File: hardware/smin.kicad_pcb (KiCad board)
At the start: 2 copper layers, 36 parts, among them P1 ISP, P2 CONN_1, Q1 BSS84, SW1 SW_DIP_8, SW2 SW_PUSH, U1 MINIMUS, U2 MINIMUS, U3 CD4050, U4 74HC243, U5 ZIF, U6 NCP1117, U7 AT45DB, X1 PIEZO

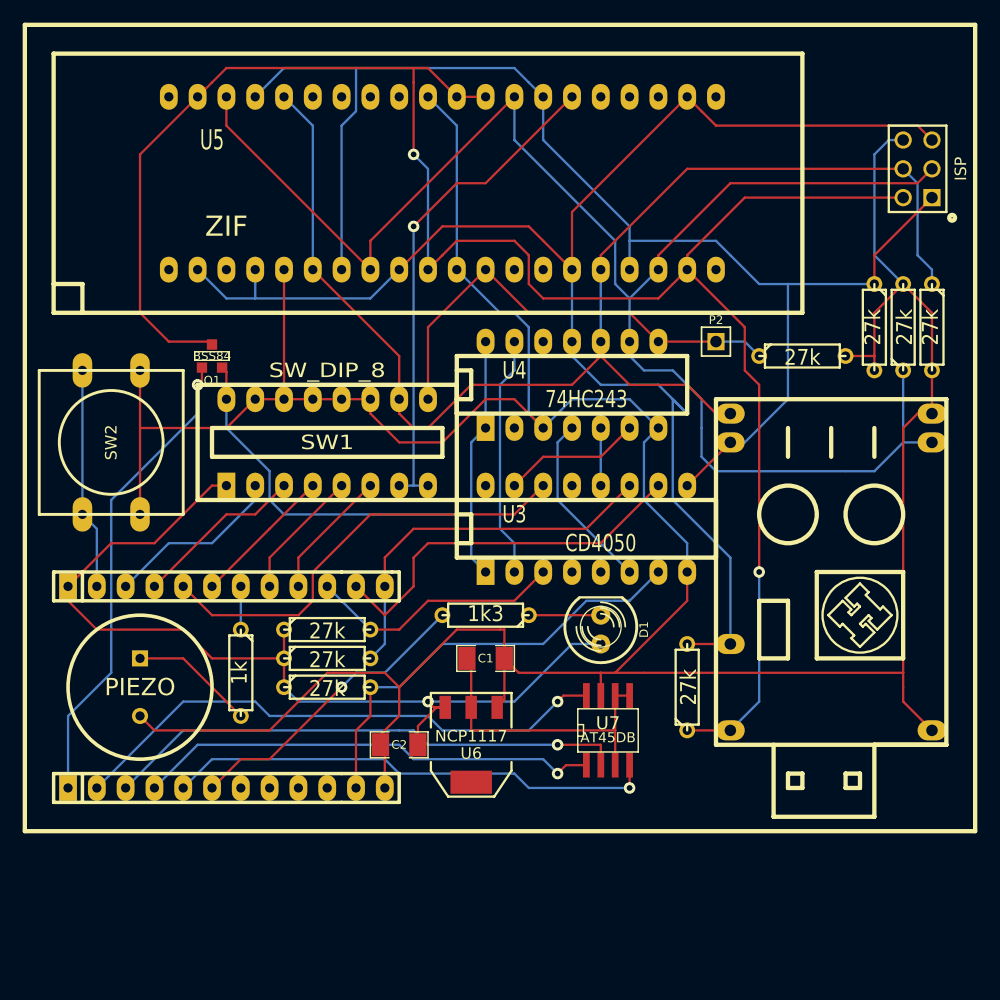
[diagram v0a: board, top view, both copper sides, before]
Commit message: PCB fixes
Signed-off-by: Paul Brook <paul@nowt.org>
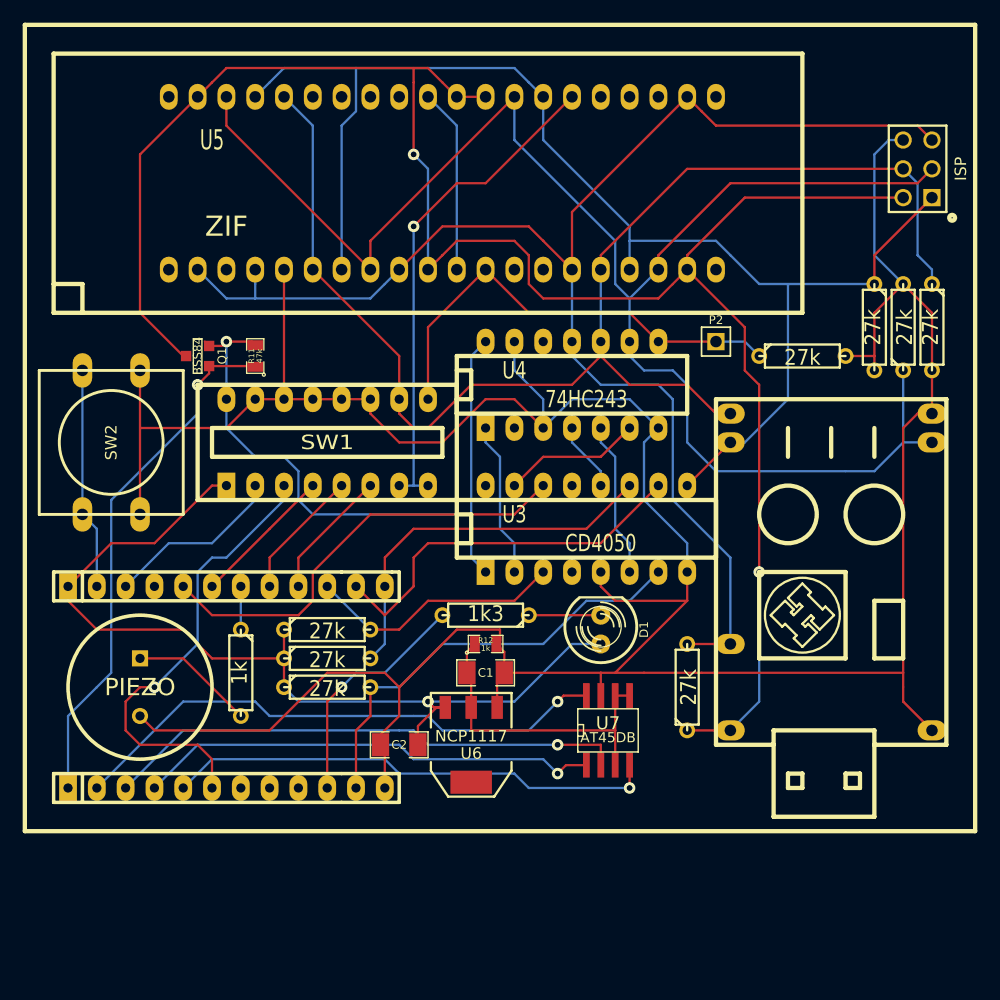
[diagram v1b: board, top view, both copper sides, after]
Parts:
- added R11: 47k, SM0805, F.Cu at (45.7, 54.6)
- added R12: 1k, SM0805, F.Cu at (66.0, 80.0)
- SW2: footprint SW_PUSH-12mm -> SW_PUSH-12
- moved LOGO_SMALL 5.08 mm to (94.0, 77.5)
- moved C1 1.27 mm to (66.0, 82.5)
- moved Q1 1.27 mm to (40.6, 54.6), turned to 270 degrees
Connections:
- R10 pad 2: N-0000026 (its old number) -> N-0000014
- U1 pad 10: (no net) -> N-0000014
- U1 pad 6: N-0000026 (its old number) -> /CFG3
- U2 pad 4: /CFG3 -> (no net)
- U3 pad 12: N-0000028 (its old number) -> N-000009
- U3 pad 5: (no net) -> GND
- U3 pad 6: N-0000013 (its old number) -> N-0000022
- U4 pad 1: /VCC -> N-0000053
- U4 pad 13: N-0000053 -> GND
- U4 pad 4: N-0000013 (its old number) -> N-000009
- U4 pad 5: N-0000028 (its old number) -> N-0000022
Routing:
- net N-0000026 (its old number): track 26.6 -> 0.00 mm, vias 1 -> 0
- net /CFG3: track 15.1 -> 40.1 mm, vias 0 -> 1
- net N-0000014: track 0.00 -> 20.9 mm, vias 0 -> 1
- net N-0000013 (its old number): track 15.9 -> 0.00 mm
- net N-0000022: track 0.00 -> 13.8 mm
- net N-0000053: track 21.4 -> 13.8 mm
- net /VCC: track 53.1 -> 60.1 mm, vias 0 -> 1
- net N-000009: track 0.00 -> 6.13 mm
- net N-0000028 (its old number): track 5.08 -> 0.00 mm
- net N-0000031: track 42.0 -> 46.5 mm
- net RST: track 132.6 -> 129.0 mm
- net +3.3V: track 26.1 -> 28.2 mm
- net Vt: track 173.6 -> 171.7 mm

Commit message: First pass at rev2 hardware
Signed-off-by: Paul Brook <paul@nowt.org>
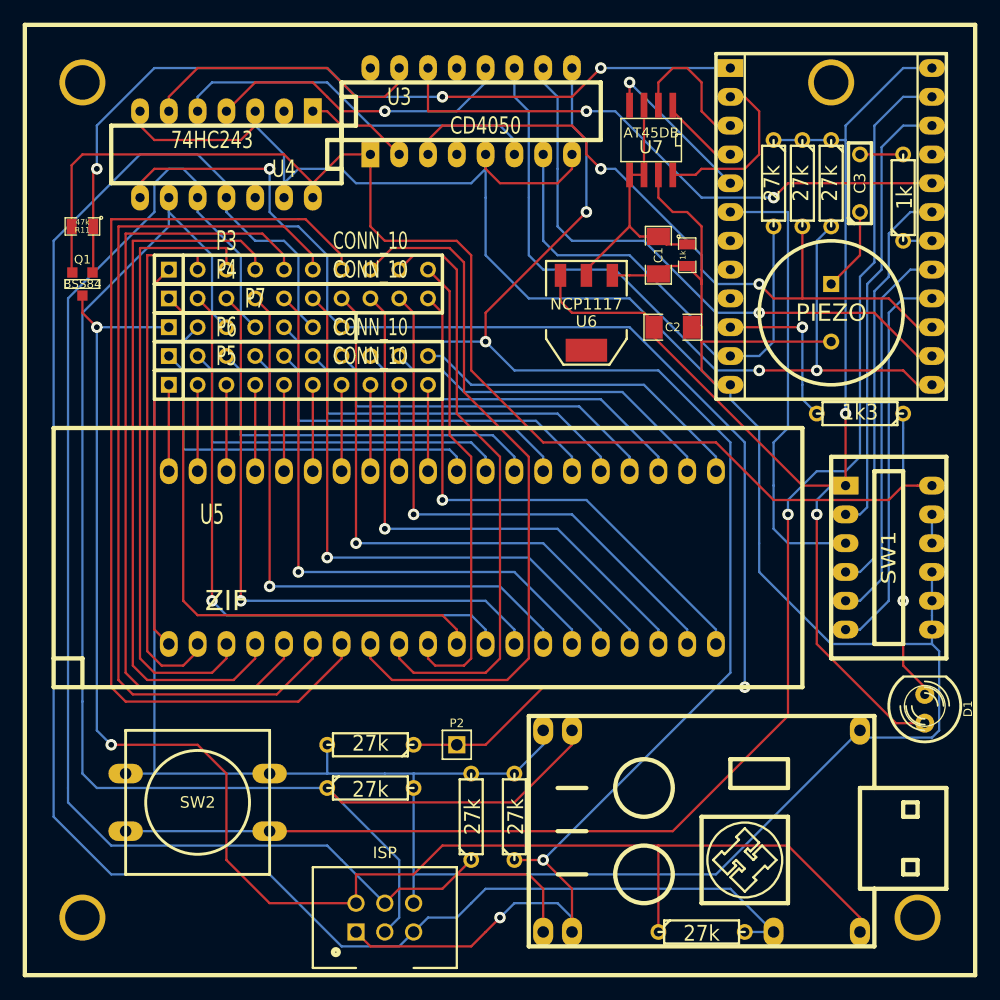
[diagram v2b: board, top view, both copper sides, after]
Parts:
- removed U2: MINIMUS, SIL-12-ELL
- added C3: 100n, C2, F.Cu at (99.1, 39.4)
- added P10: CONN_1, HOLE3, F.Cu at (96.5, 30.5)
- added P11: CONN_1, HOLE3, F.Cu at (30.5, 30.5)
- added P3: CONN_10, SIL-10, F.Cu at (49.5, 47.0)
- added P4: CONN_10, SIL-10, F.Cu at (49.5, 49.5)
- added P5: CONN_10, SIL-10, F.Cu at (49.5, 57.1)
- added P6: CONN_10, SIL-10, F.Cu at (49.5, 54.6)
- added P7: CONN_7, SIL-7, F.Cu at (45.7, 52.1)
- added P8: CONN_1, HOLE3, F.Cu at (104.1, 104.1)
- added P9: CONN_1, HOLE3, F.Cu at (30.5, 104.1)
- P1: footprint pin_array_3x2 -> AVRISP6
- SW1: value SW_DIP_8 -> SW_DIP_6; footprint SWDIP8 -> SWDIP6
- U1: footprint SIL-12-ELL -> MINIMUS
- moved P1 81.1 mm to (57.1, 104.1), turned to 0 degrees
- moved U1 72.8 mm to (96.5, 43.2), turned to 270 degrees
- moved R4 71.9 mm to (102.9, 40.6), turned to 90 degrees
- moved X1 69.3 mm to (96.5, 50.8)
- moved R7 62.1 mm to (55.9, 92.7), turned to 0 degrees
- moved R2 61.1 mm to (96.5, 39.4), turned to 270 degrees
- moved R3 59.4 mm to (91.4, 39.4), turned to 270 degrees
- moved R6 59.3 mm to (64.8, 95.2), turned to 90 degrees
- moved G*** 59.2 mm to (45.7, 73.7)
- moved R1 57.5 mm to (94.0, 39.4), turned to 270 degrees
- moved R8 53.6 mm to (68.6, 95.2), turned to 90 degrees
- moved U7 52.3 mm to (81.3, 35.6), turned to 180 degrees
- moved R9 51.3 mm to (55.9, 88.9), turned to 180 degrees
- moved SW1 50.6 mm to (101.6, 72.4), turned to 270 degrees
- moved TP12 48.6 mm to (71.1, 105.4), turned to 90 degrees
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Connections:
- R1 pad 2: N-0000013 -> N-0000080
- R2 pad 2: N-0000011 -> N-0000055
- R4 pad 1: N-0000012 -> N-0000078
- SW1 pad 10: MOSI -> GND
- SW1 pad 12: GND -> /VCC
- SW1 pad 7: /MX -> GND
- SW1 pad 8: /MX -> GND
- SW1 pad 9: XCK -> GND
- U3 pad 10: N-0000028 -> N-0000017
- U3 pad 11: N-0000011 -> N-0000055
- U3 pad 14: N-0000010 (its old number) -> N-0000057
- U3 pad 3: N-0000013 -> N-0000080
- U5 pad 1: (no net) -> N-0000059
- U5 pad 10: Vt -> N-0000067
- U5 pad 11: GND -> N-0000053
- U5 pad 12: XCK -> N-0000051
- U5 pad 13: (no net) -> N-0000049
- U5 pad 14: (no net) -> N-0000050
- U5 pad 15: RST -> N-0000048
- U5 pad 16: MOSI -> N-0000047
- U5 pad 17: MISO -> N-0000046
- U5 pad 18: SCK -> N-0000045
- U5 pad 19: Vt -> N-0000044
- U5 pad 2: RST -> N-0000060
- U5 pad 20: (no net) -> N-0000043
- U5 pad 21: (no net) -> N-0000042
- U5 pad 22: RST -> N-0000041
- U5 pad 23: (no net) -> N-0000040
- U5 pad 24: (no net) -> N-0000039
- U5 pad 25: (no net) -> N-0000038
- U5 pad 26: /MX -> N-0000037
- U5 pad 27: MISO -> N-0000029
- U5 pad 28: SCK -> N-0000021
- U5 pad 29: Vt -> N-0000022
- U5 pad 3: (no net) -> N-0000058
- U5 pad 30: Vt -> N-0000023
- U5 pad 31: GND -> N-0000024
- U5 pad 32: (no net) -> N-0000025
- U5 pad 33: (no net) -> N-0000026
- U5 pad 34: (no net) -> N-0000027
- U5 pad 35: (no net) -> N-0000028
- U5 pad 36: MOSI -> N-0000020
- U5 pad 37: MISO -> N-0000030
- U5 pad 38: SCK -> N-0000031
- U5 pad 39: Vt -> N-0000032
- U5 pad 4: RST -> N-0000061
- U5 pad 40: (no net) -> N-0000033
- U5 pad 5: GND -> N-0000062
- U5 pad 6: MOSI -> N-0000063
- U5 pad 7: MISO -> N-0000064
- U5 pad 8: SCK -> N-0000065
- U5 pad 9: RST -> N-0000066
- X1 pad 1: N-0000052 -> N-0000077
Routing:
- net /CFG1: track 19.6 -> 125.5 mm, vias 0 -> 1
- net N-0000064: track 0.00 -> 87.9 mm
- net XCK: track 40.8 -> 123.2 mm, vias 0 -> 2
- net N-0000063: track 0.00 -> 79.7 mm
- net N-0000062: track 0.00 -> 71.6 mm
- net N-0000055: track 0.00 -> 70.6 mm, vias 0 -> 2
- net N-0000065: track 0.00 -> 63.7 mm
- net N-0000061: track 0.00 -> 63.4 mm
- net N-0000080: track 0.00 -> 61.4 mm, vias 0 -> 2
- net N-0000058: track 0.00 -> 55.7 mm
- net N-0000053: track 0.00 -> 53.6 mm
- net N-0000051: track 0.00 -> 53.6 mm, vias 0 -> 1
- net N-0000049: track 0.00 -> 53.6 mm, vias 0 -> 1
- net N-0000066: track 0.00 -> 53.2 mm
- net N-0000050: track 0.00 -> 52.9 mm, vias 0 -> 1
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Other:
- board text added: "Rev 2"
- board text removed: "tiny2313"
- board text removed: "tiny5"
- board text removed: "tiny6"
- board text removed: "tiny8/mega8"
